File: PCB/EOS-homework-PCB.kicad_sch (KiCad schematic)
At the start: 0 parts

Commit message: Generate project from template
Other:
- title: template_pretty_name -> EOS Homework Board
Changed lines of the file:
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@@
 	(paper "A4")
 	(title_block
-		(title "template_pretty_name")
+		(title "EOS Homework Board")
 	)
 	(no_connect

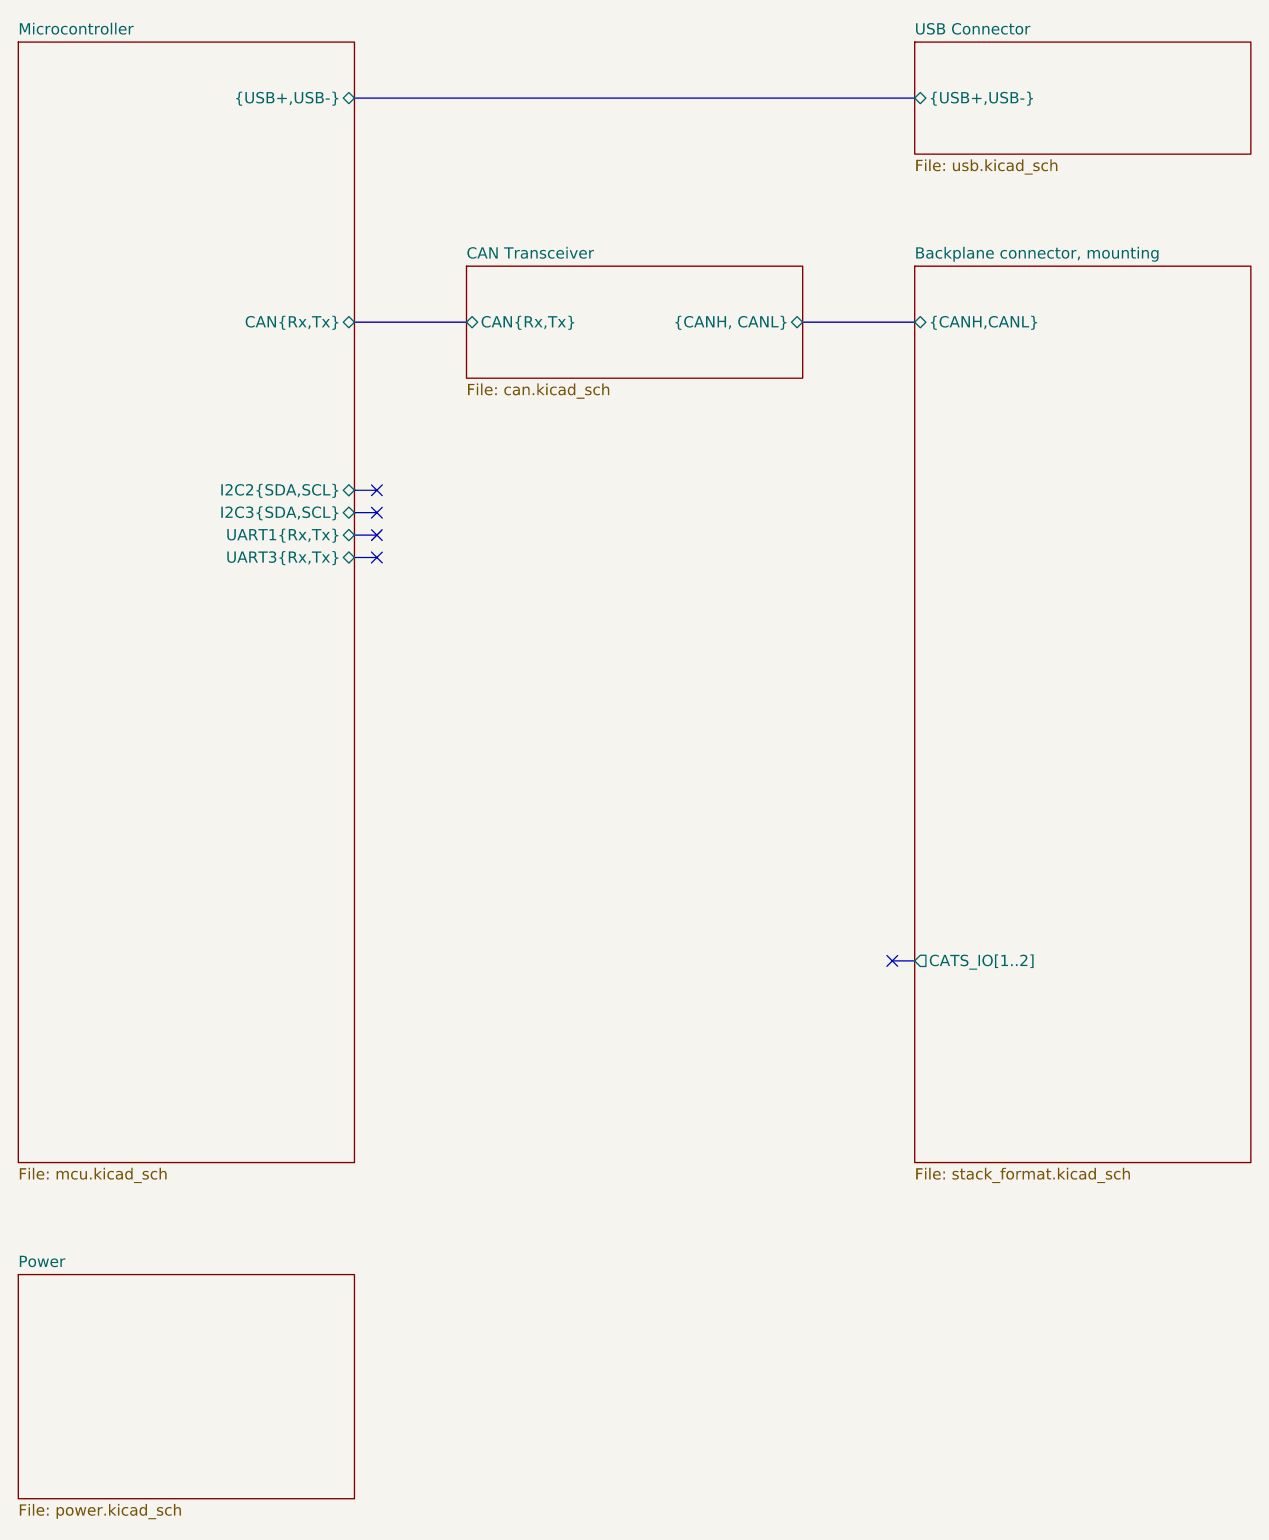
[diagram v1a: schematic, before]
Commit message: Schematic done
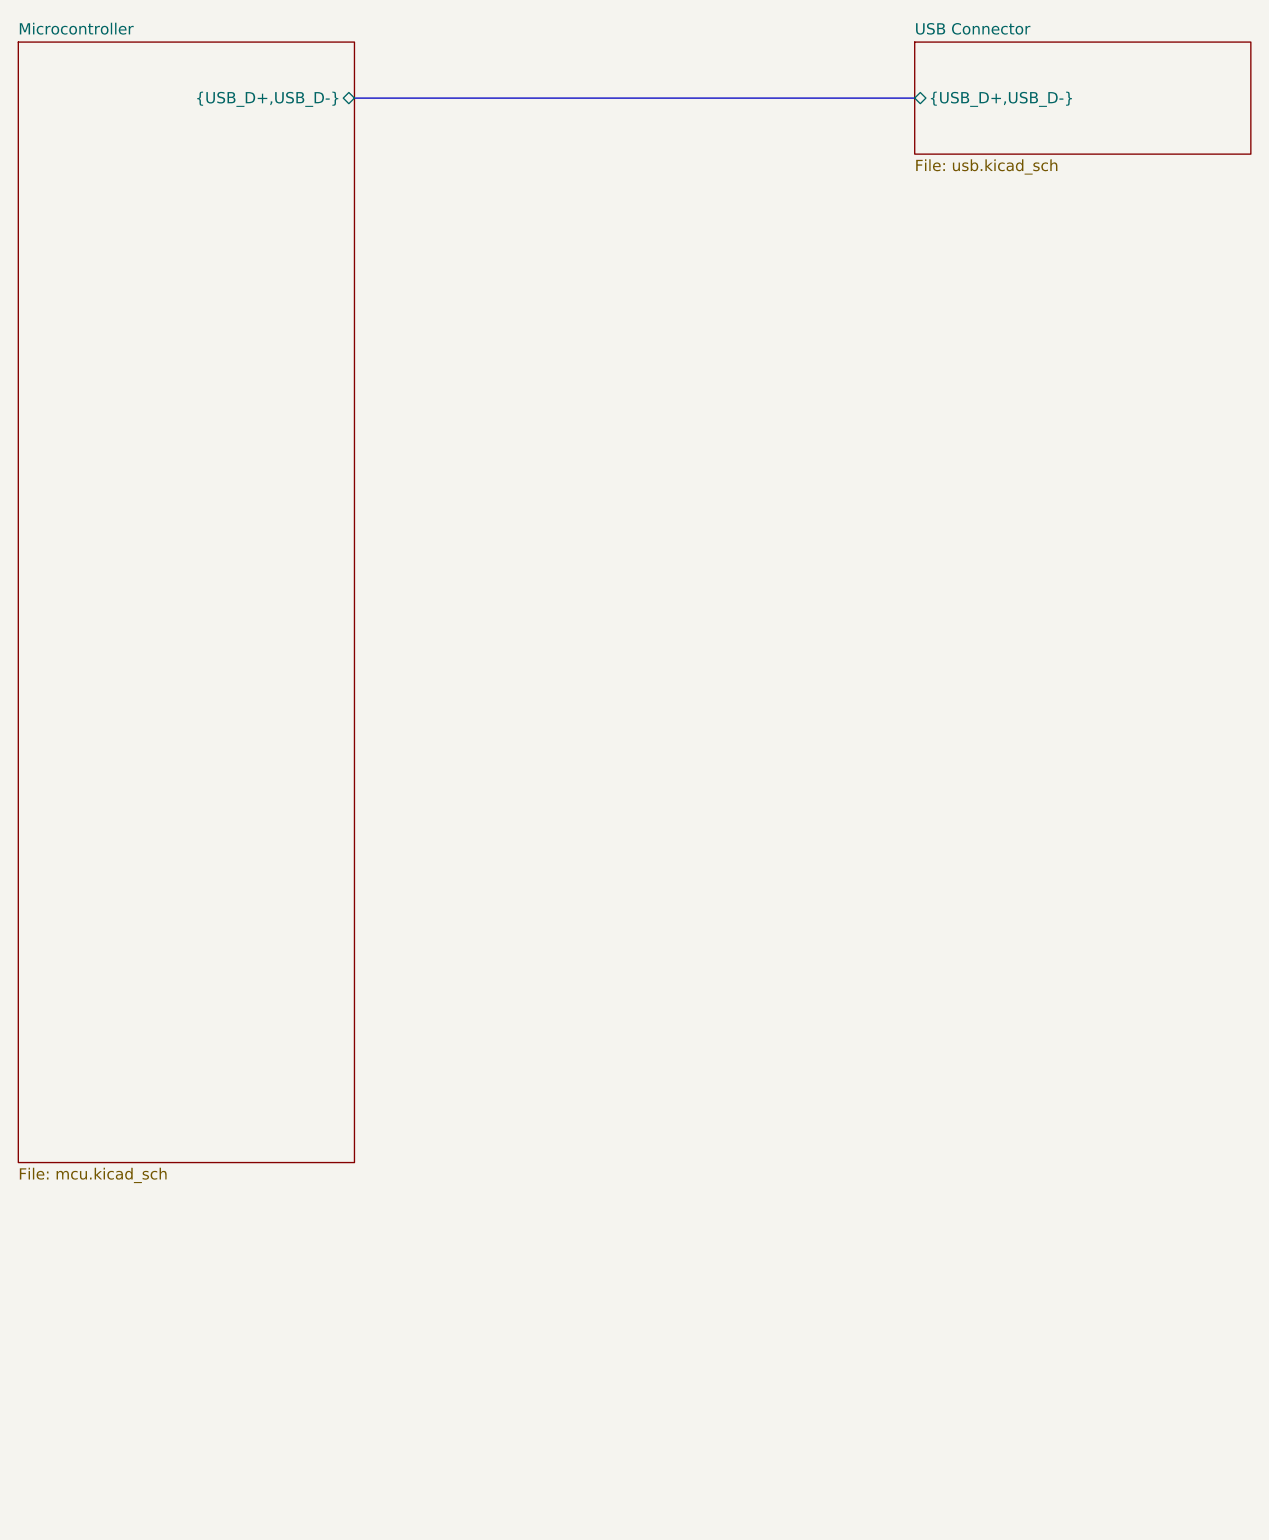
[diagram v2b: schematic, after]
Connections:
- no-connect marks 5 -> 0
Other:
- removed sheet Backplane connector, mounting
- removed sheet CAN Transceiver
- removed sheet Power
- sheet Microcontroller ports: added {USB_D+,USB_D-}; removed CAN{Rx,Tx}, I2C2{SDA,SCL}, I2C3{SDA,SCL}, UART1{Rx,Tx}, UART3{Rx,Tx}, {USB+,USB-}
- sheet USB Connector ports: added {USB_D+,USB_D-}; removed {USB+,USB-}

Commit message: PCB done.
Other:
- removed sheet USB Connector
- sheet Microcontroller ports: added none; removed {USB_D+,USB_D-}
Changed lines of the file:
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@@
 	(title_block
 		(title "EOS Homework Board")
-		(date "2026-09-28")
+		(date "2026-09-29")
 		(rev "0.1")
 		(comment 1 "dcarocci")
-	)
-	(bus
-		(pts
-			(xy 114.3 31.75) (xy 177.8 31.75)
-		)
-		(stroke
-			(width 0)
-			(type default)
-		)
-	)
-	(sheet
-		(at 177.8 25.4)
-		(size 38.1 12.7)
-		(exclude_from_sim no)
-		(in_bom yes)
-		(on_board yes)
-		(dnp no)
-		(fields_autoplaced yes)
-		(stroke
-			(width 0.1524)
-			(type solid)
-		)
-		(fill
-			(color 0 0 0 0)
-		)
-		(property "Sheetname" "USB Connector"
-			(at 177.8 24.6884 0)
-			(show_name no)
-			(do_not_autoplace no)
-			(effects
-				(font
-					(size 1.27 1.27)
-				)
-				(justify left bottom)
-			)
-		)
-		(property "Sheetfile" "usb.kicad_sch"
-			(at 177.8 38.6846 0)
-			(show_name no)
-			(do_not_autoplace no)
-			(effects
-				(font
-					(size 1.27 1.27)
-				)
-				(justify left top)
-			)
-		)
-		(pin "{USB_D+,USB_D-}" bidirectional
-			(at 177.8 31.75 180)
-			(effects
-				(font
-					(size 1.27 1.27)
-				)
-				(justify left)
-			)
-		)
-		(instances
-			(project "EOS-homework-PCB"
-				(path "/e08d3e09-d805-4650-baae-a4ad395cf0c7"
-					(page "5")
-				)
-			)
-		)
 	)
 	(sheet
@@
 			)
 		)
-		(pin "{USB_D+,USB_D-}" bidirectional
-			(at 114.3 31.75 0)
-			(effects
-				(font
-					(size 1.27 1.27)
-				)
-				(justify right)
-			)
-		)
